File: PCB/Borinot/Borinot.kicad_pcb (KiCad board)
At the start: 2 copper layers, 41.9 x 35.4 mm, 31 parts, among them J1 USB_C_Receptacle_USB2.0, J2 Battery, J3 HumiditySensor, U1 MCP73871-2CC

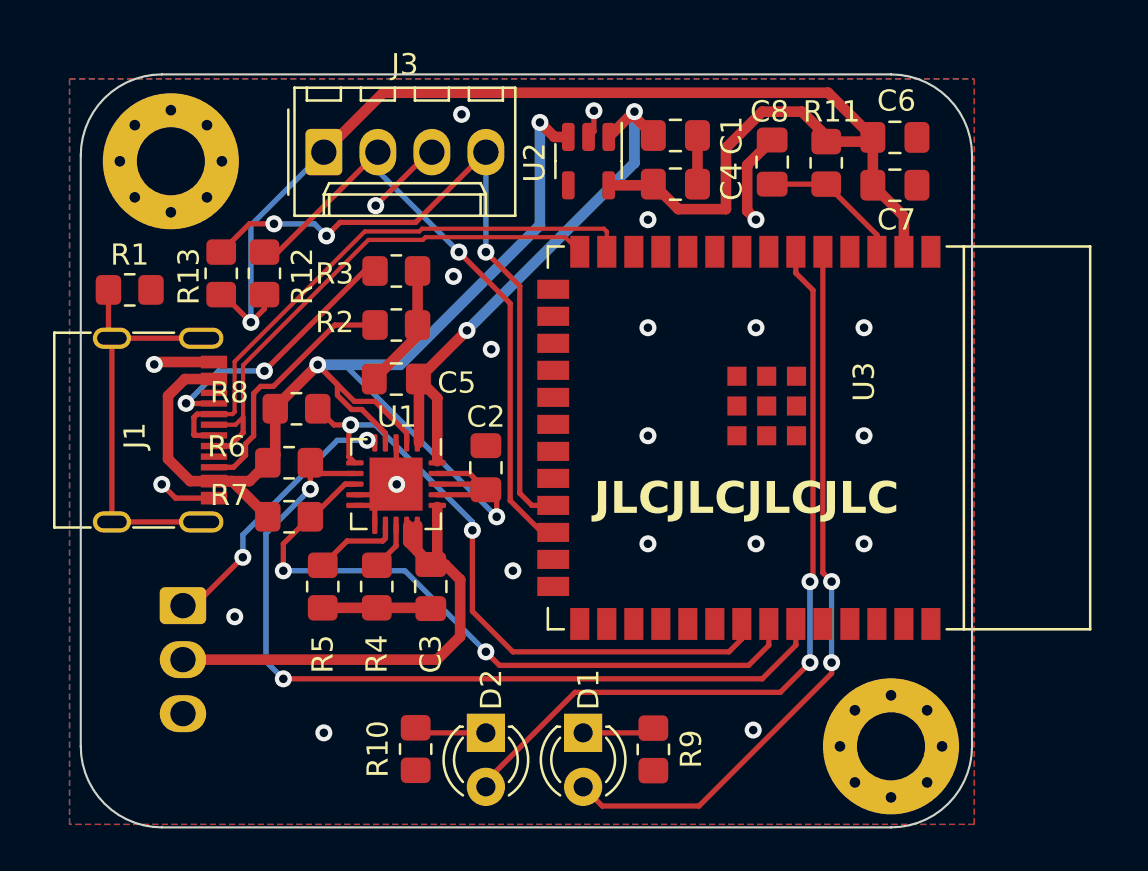
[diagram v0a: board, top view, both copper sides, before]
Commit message: Four-layer board
Moved the design to a four-layer board, to simplify routing.
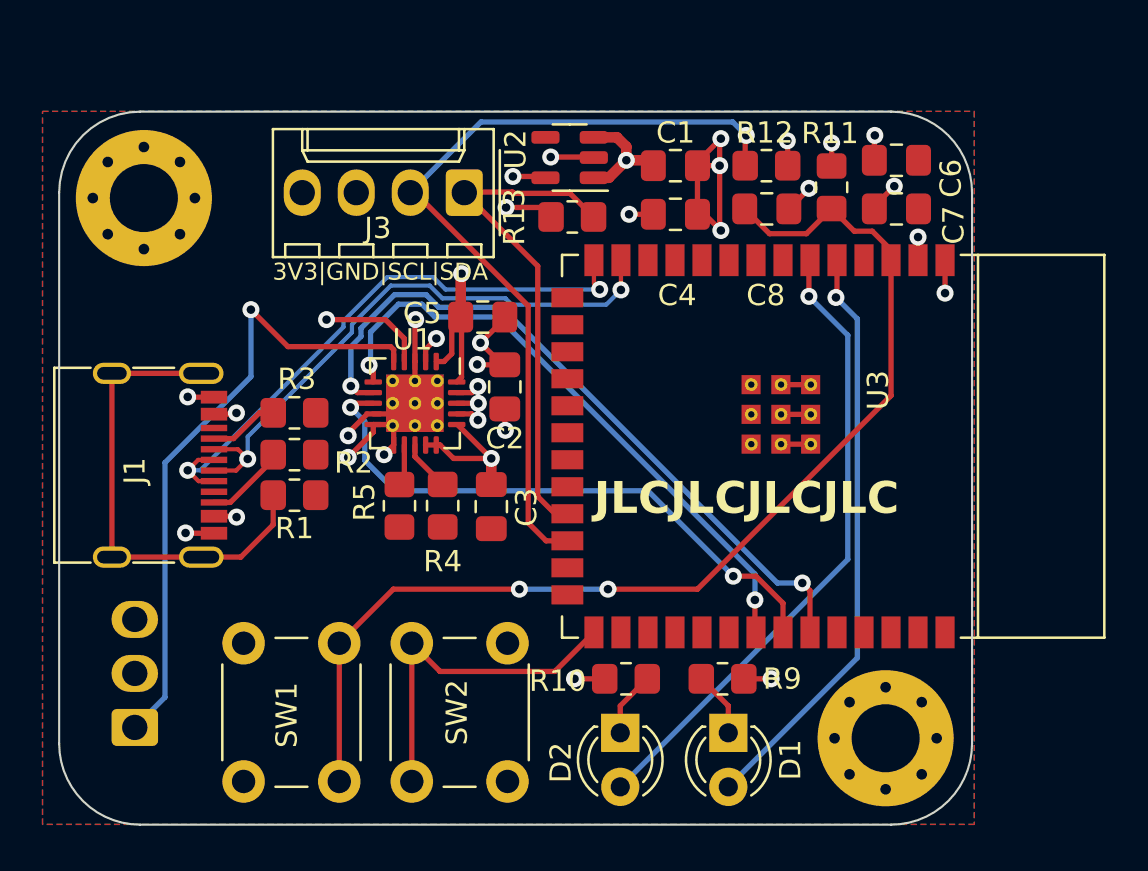
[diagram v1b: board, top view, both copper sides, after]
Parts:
- removed R6, R7, R8: 470, Resistor_SMD:R_0805_2012Metric_Pad1.20x1.40mm_HandSolder
- added SW1: RESET, Button_Switch_THT:SW_PUSH_6mm, F.Cu at (140.4, 111.4)
- added SW2: PROG, Button_Switch_THT:SW_PUSH_6mm, F.Cu at (143.8, 117.9)
- U1: footprint Package_DFN_QFN:QFN-20-1EP_4x4mm_P0.5mm_EP2.5x2.5mm -> Package_DFN_QFN:TQFN-20-1EP_4x4mm_P0.5mm_EP2.7x2.7mm_ThermalVias
- moved R12 24.1 mm to (160.5, 88.9), turned to 180 degrees
- moved R13 16.7 mm to (151.4, 91.3), turned to 0 degrees
- moved R1 12.4 mm to (138.3, 104.4)
- moved R10 10.4 mm to (153.9, 113.0), turned to 180 degrees
- moved R3 8.21 mm to (138.3, 100.5)
- moved R2 7.75 mm to (138.3, 102.5)
- moved J3 6.87 mm to (146.3, 90.2), turned to 180 degrees
- moved D1 6.83 mm to (158.7, 115.6)
- moved D2 6.32 mm to (153.6, 115.6)
- moved J2 6.16 mm to (130.8, 115.3), turned to 90 degrees
- moved R5 5.24 mm to (143.3, 104.9)
- moved C5 5.00 mm to (147.2, 96.0), turned to 0 degrees
- moved R4 4.91 mm to (145.3, 104.9)
- moved C3 4.71 mm to (147.6, 104.9)
- moved R9 4.65 mm to (158.4, 113.0), turned to 0 degrees
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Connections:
- net /ESP_EN renamed ESP_EN
- C1 pad 1: Net-(U2-VIN) -> BAT_OUT
- C5 pad 1: Net-(U2-VIN) -> BAT_OUT
- J3 pad 1: VDD33 -> ESP_SDA
- J3 pad 4: ESP_SDA -> VDD33
- U1 pad 1: Net-(U2-VIN) -> BAT_OUT
- U1 pad 20: Net-(U2-VIN) -> BAT_OUT
- U2 pad 1: Net-(U2-VIN) -> BAT_OUT
- U2 pad 3: USB_5V -> BAT_OUT
- U3 pad 27: unconnected-(U3-IO0-Pad27) -> GPIO0
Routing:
- net USB_5V: track 70.8 -> 12.8 mm, vias 3 -> 8
- net VDD33: track 64.1 -> 10.1 mm, vias 1 -> 8
- net ESP_EN: track 6.71 -> 52.3 mm, vias 0 -> 2
- net Net-(U2-VIN): track 27.2 -> 0.00 mm, vias 2 -> 0
- net BAT_OUT: track 0.00 -> 22.5 mm, vias 0 -> 2
- net BAT_TEMP: track 12.9 -> 30.0 mm, vias 2 -> 1
- net GPIO0: track 0.00 -> 16.4 mm
- net VBAT: track 25.0 -> 37.8 mm, vias 0 -> 1
- net ESP_SDA: track 33.4 -> 23.4 mm, vias 3 -> 0
- net ESP_SCL: track 28.9 -> 38.8 mm
- net /USB_CC1: track 12.8 -> 3.29 mm, vias 2 -> 0
- net /USB_CC2: track 11.8 -> 3.62 mm
- net LOW_BAT: track 37.5 -> 29.9 mm, vias 2 -> 1
- net CHARGE: track 34.6 -> 27.7 mm, vias 2 -> 1
- net BAT_STAT2: track 39.4 -> 33.6 mm
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- added copper zone on In1.Cu, net GND
- added copper zone on In2.Cu, net USB_5V
- added copper zone on In2.Cu, net VDD33
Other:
- board size 41.9 x 35.4 mm -> 42.9 x 33.5 mm
- copper layers 2 -> 4
- board text added: "3V3|GND|SCL|SDA"
- board text added: "Borinot v0.2 Pau Estalella 2023-04-01"
- board text added: "GND"
- board text added: "THERM"
- board text added: "VBAT"
- board text removed: "Borinot v0.1 Pau Estalella 2023-03-07"

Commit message: Battery management change
Use an easier-to-solder SOT-23-5-packaged battery manager
to simplify the soldeering of the PCBs.
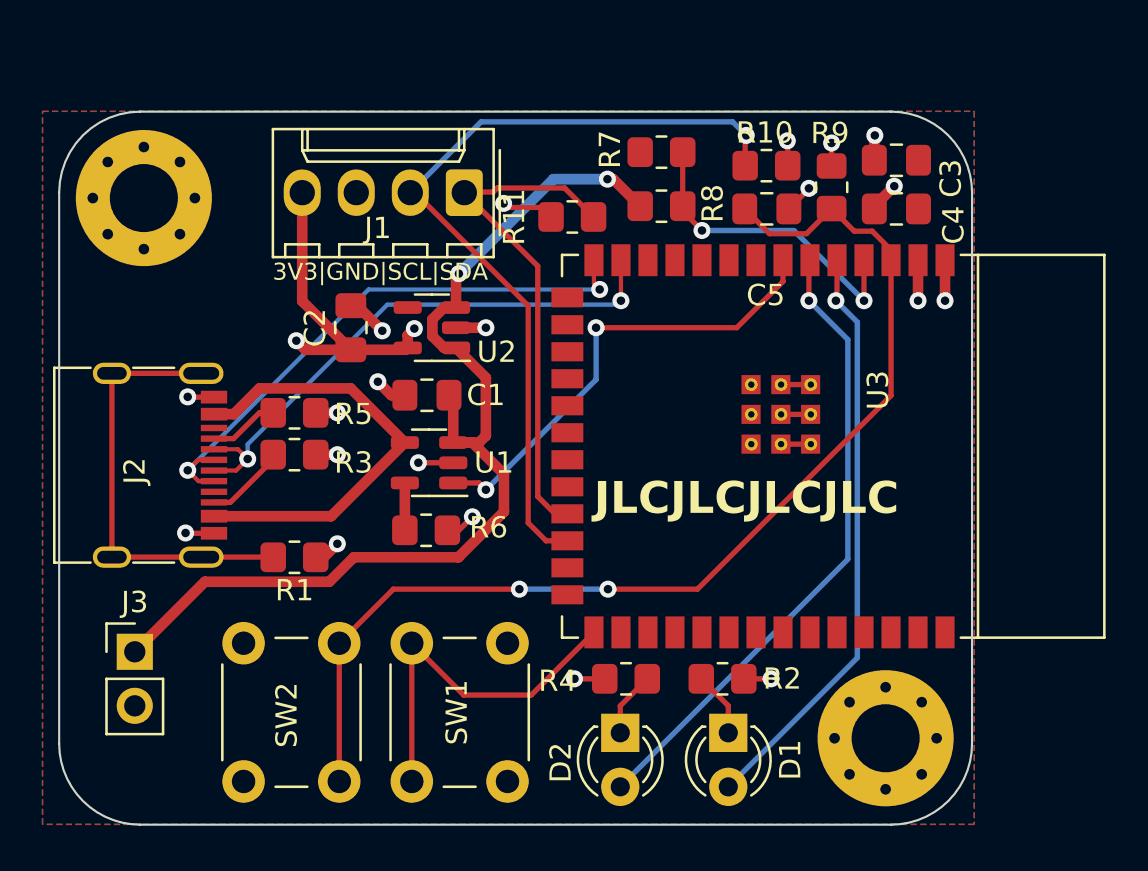
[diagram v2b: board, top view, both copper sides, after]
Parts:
- removed the C3 at (147.6, 104.9)
- removed the C4 at (156.2, 91.2)
- removed the C5 at (147.2, 96.0)
- removed the J2 at (130.8, 115.3)
- removed the R4 at (145.3, 104.9)
- removed the R5 at (143.3, 104.9)
- added J3: Battery, Connector_PinHeader_2.54mm:PinHeader_1x02_P2.54mm_Vertical, F.Cu at (130.8, 111.8)
- added R6: 2k, Resistor_SMD:R_0805_2012Metric_Pad1.20x1.40mm_HandSolder, F.Cu at (144.5, 106.0)
- added R7: 100k, Resistor_SMD:R_0805_2012Metric_Pad1.20x1.40mm_HandSolder, F.Cu at (155.6, 90.8)
- added R8: 100k, Resistor_SMD:R_0805_2012Metric_Pad1.20x1.40mm_HandSolder, F.Cu at (155.6, 88.3)
- C2: value 10uF -> 1uF
- U1: value MCP73871-2CC -> MCP73812T-420I-OT; footprint Package_DFN_QFN:TQFN-20-1EP_4x4mm_P0.5mm_EP2.7x2.7mm_ThermalVias -> Package_TO_SOT_SMD:SOT-23-5
- moved C1 15.9 mm to (144.5, 99.7), turned to 180 degrees
- moved U2 10.3 mm to (144.8, 96.5)
- moved C2 7.75 mm to (141.0, 96.5)
- moved R1 2.92 mm to (138.3, 107.3)
- moved U1 2.88 mm to (144.6, 102.9), turned to 180 degrees
- renumbered C6 to C3, C7 to C4, C8 to C5, H2 to H1, H1 to H2, J3 to J1, J1 to J2, R12 to R10, R13 to R11, R9 to R2, R2 to R3, R10 to R4, R3 to R5, R11 to R9, SW2 to SW1, SW1 to SW2
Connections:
- C1 pad 1: BAT_OUT -> VBAT
- C2 pad 1: USB_5V -> VDD33
- U1 pad 1: BAT_OUT -> BAT_CE
- U1 pad 2: USB_5V -> GND
- U1 pad 3: GND -> VBAT
- U1 pad 5: BAT_TEMP -> Net-(U1-PROG)
- U2 pad 1: BAT_OUT -> VBAT
- U2 pad 3: BAT_OUT -> VBAT
- U3 pad 33: ~{BAT_PG} -> unconnected-(U3-IO40-Pad33)
- U3 pad 34: ~{BAT_LBO} -> unconnected-(U3-IO41-Pad34)
- U3 pad 35: BAT_STAT2 -> unconnected-(U3-IO42-Pad35)
- U3 pad 4: unconnected-(U3-IO4-Pad4) -> BAT_SENSE
- U3 pad 7: unconnected-(U3-IO7-Pad7) -> BAT_CE
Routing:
- net BAT_STAT2: track 33.6 -> 0.00 mm, vias 2 -> 0
- net BAT_TEMP: track 30.0 -> 0.00 mm, vias 1 -> 0
- net ~{BAT_PG}: track 29.0 -> 0.00 mm, vias 2 -> 0
- net ~{BAT_LBO}: track 27.7 -> 0.00 mm, vias 2 -> 0
- net BAT_OUT: track 22.5 -> 0.00 mm, vias 2 -> 0
- net BAT_CE: track 0.00 -> 22.1 mm, vias 0 -> 2
- net GND: track 40.7 -> 24.0 mm, vias 16 -> 14
- net BAT_SENSE: track 0.00 -> 15.0 mm, vias 0 -> 2
- net VDD33: track 10.1 -> 23.5 mm
- net VBAT: track 37.8 -> 49.6 mm, vias 1 -> 2
- net USB_5V: track 12.8 -> 20.9 mm, vias 8 -> 0
- net BAT_PROG1: track 2.39 -> 0.00 mm
- net Net-(U1-PROG): track 0.00 -> 2.23 mm
- net Net-(J2-SHIELD): track 22.5 -> 20.4 mm
- net BAT_PROG3: track 1.63 -> 0.00 mm
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- removed copper zone on In2.Cu, net USB_5V
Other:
- board text added: "Borinot v0.3 Pau Estalella 2023-05-02"
- board text removed: "Borinot v0.2 Pau Estalella 2023-04-01"
- board text removed: "THERM"

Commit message: Add missing pull-up on ChargeEnable pin
Without a pull-up to USB 5V on that pin it is impossible
to start the ESP32 when the battery is below 3.3V
Added a voltage divider to sense the 5V from USB and
be able to decide whether to charge the battery or not.
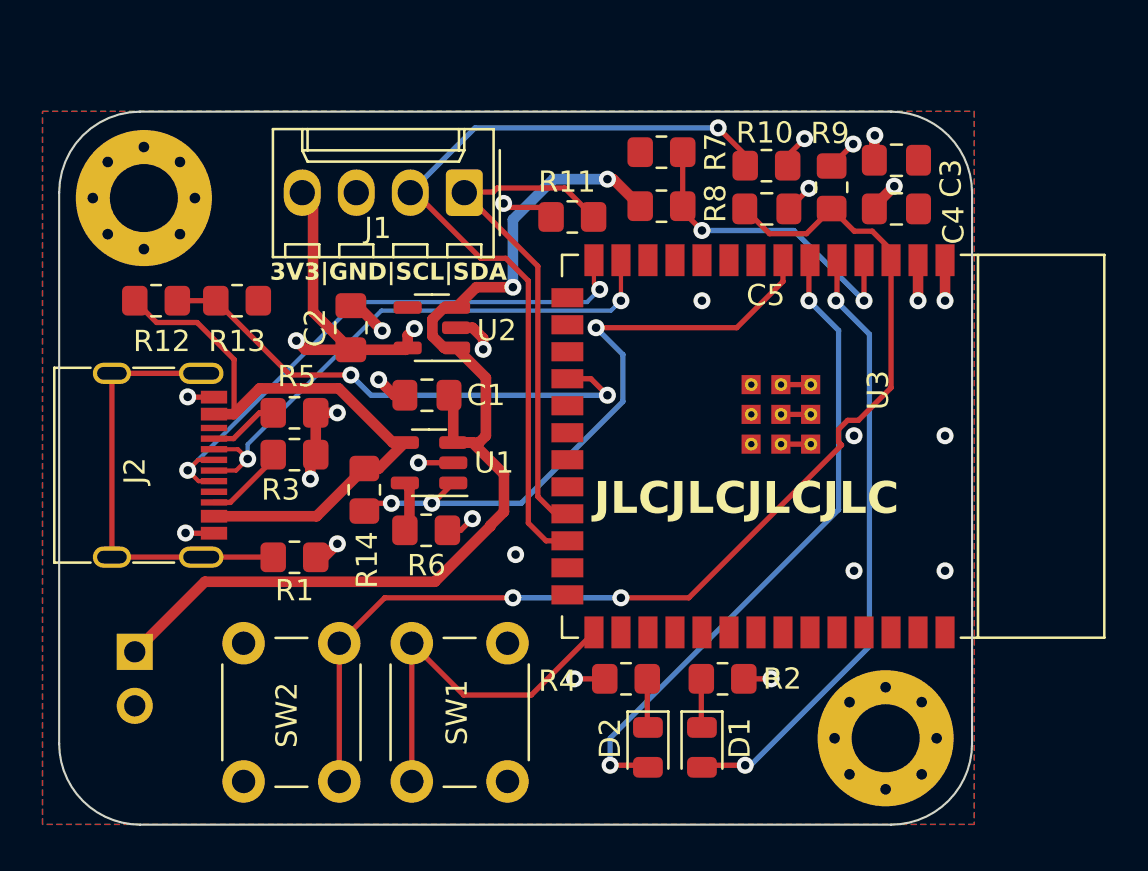
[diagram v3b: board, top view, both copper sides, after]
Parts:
- added R12: 5k, Resistor_SMD:R_0805_2012Metric_Pad1.20x1.40mm_HandSolder, F.Cu at (131.8, 95.2)
- added R13: 10k, Resistor_SMD:R_0805_2012Metric_Pad1.20x1.40mm_HandSolder, F.Cu at (135.6, 95.2)
- added R14: 10k, Resistor_SMD:R_0805_2012Metric_Pad1.20x1.40mm_HandSolder, F.Cu at (141.6, 104.1)
- D1, D2: footprint LED_THT:LED_D3.0mm -> LED_SMD:LED_0805_2012Metric
- J3: moved to B.Cu
- moved D2 1.47 mm to (154.9, 116.3)
- moved D1 1.41 mm to (157.5, 116.3)
- turned J3 to 180 degrees
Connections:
- U3 pad 18: unconnected-(U3-IO10-Pad18) -> USB_SENSE
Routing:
- net USB_SENSE: track 0.00 -> 24.3 mm, vias 0 -> 2
- net USB_5V: track 20.9 -> 30.2 mm
- net BAT_CE: track 22.1 -> 30.4 mm, vias 2 -> 3
- net GND: track 24.0 -> 26.8 mm, vias 14 -> 20
- net CHARGE: track 27.7 -> 29.1 mm, vias 1 -> 2
- net VBAT: track 49.6 -> 50.6 mm
- net VDD33: track 23.5 -> 24.3 mm
- net Net-(D1-K): track 3.07 -> 2.30 mm
- net Net-(D2-K): track 3.07 -> 2.30 mm
- net LOW_BAT: track 29.9 -> 30.5 mm, vias 1 -> 2
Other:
- board text added: "Borinot v0.4 Pau Estalella 2023-05-20"
- board text removed: "Borinot v0.3 Pau Estalella 2023-05-02"
